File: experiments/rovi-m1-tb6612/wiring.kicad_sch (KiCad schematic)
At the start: 4 parts, among them M1 DC_MOTOR, U1 ESP32S3, U2 TB6612FNG

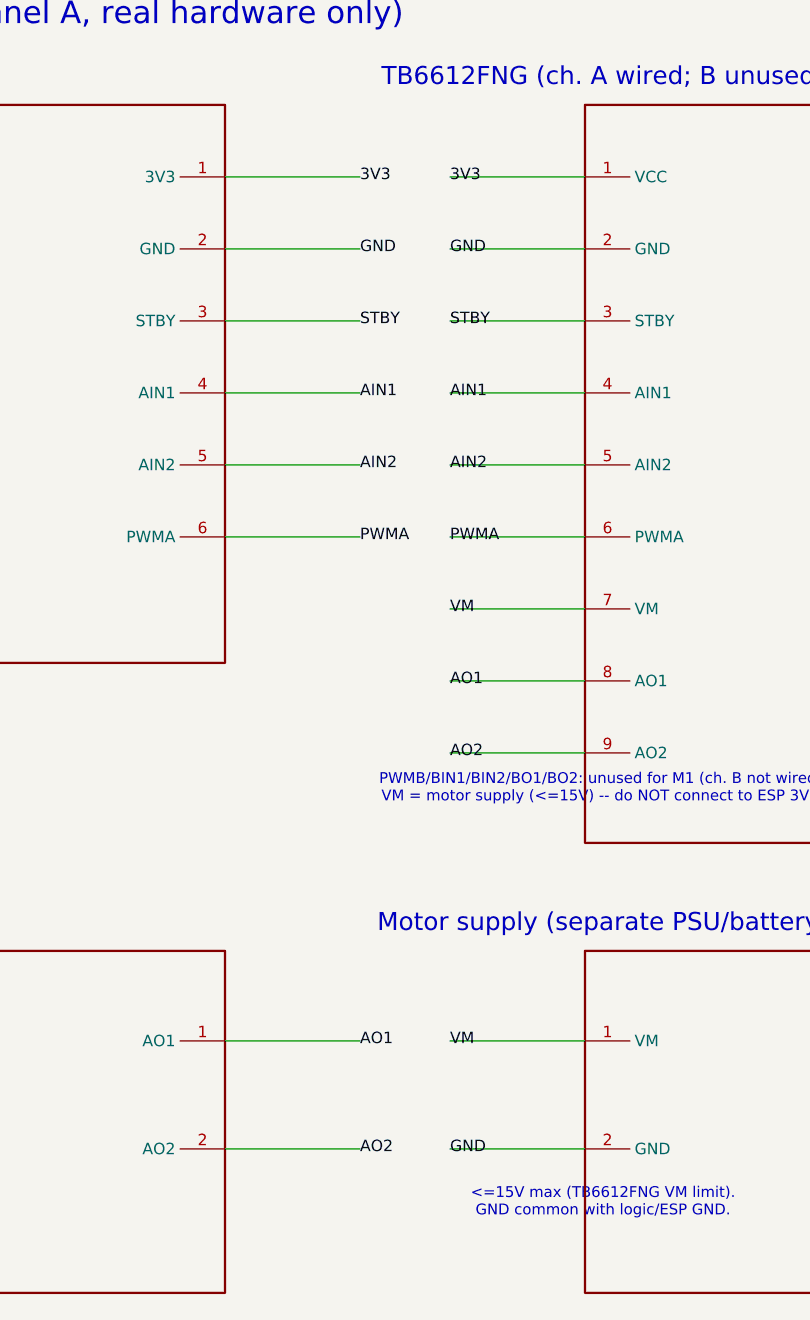
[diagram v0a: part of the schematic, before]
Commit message: wiring.kicad_sch: draw real wires between components, not just labels
The previous version connected pins purely via matching net labels
(electrically valid -- 0 ERC errors, confirmed real wire strokes in
the exported SVG) but never drew a line between the actual component
boxes. Opened in KiCad, that reads as floating labels near each pin,
not "wires connecting my components" -- a fair complaint.

Replaced the per-pin wire-to-label stubs with real point-to-point
wires: direct straight lines between ESP32S3 and TB6612FNG for the six
shared signals (3V3/GND/STBY/AIN1/AIN2/PWMA -- their pins happen to
share row Y-coordinates, so these are literal straight lines), and
bent multi-segment wires routing VM/AO1/AO2 from TB6612FNG down to the
Motor and Motor-supply boxes. GND is a 3-point net (ESP + TB6612FNG +
motor supply) so it gets an actual wire junction (visible dot) rather
than a fourth label.

Hit and diagnosed a real kicad-cli 9.0.6 ERC bug along the way: for a
direct multi-symbol wire with no label on it, `sch erc` always flags
the *first* point in a wire's `pts` list as "wire_dangling", regardless
of what's actually there -- confirmed by reversing the point order and
watching the false flag move with it. Isolated via a string of minimal
repro files (angle, pin type, rectangle coords, symbol name, instance
order, and UUIDs all ruled out one at a time) before finding the
workaround: a single label anywhere on a wire (even multi-segment,
junction-branched ones) satisfies the check for the whole connected
run. Kept one small label per net for this reason and because it aids
readability, even though the wires themselves now carry the
connection.

Verified: kicad-cli sch erc -- 0 errors, 0 dangling/unconnected
warnings (down from an intermediate 9 errors while chasing the false
positive). Re-rendered to PDF and visually confirmed continuous wire
lines run between every component, including the GND junction dot.

Co-Authored-By: Claude Sonnet 5 <noreply@anthropic.com>
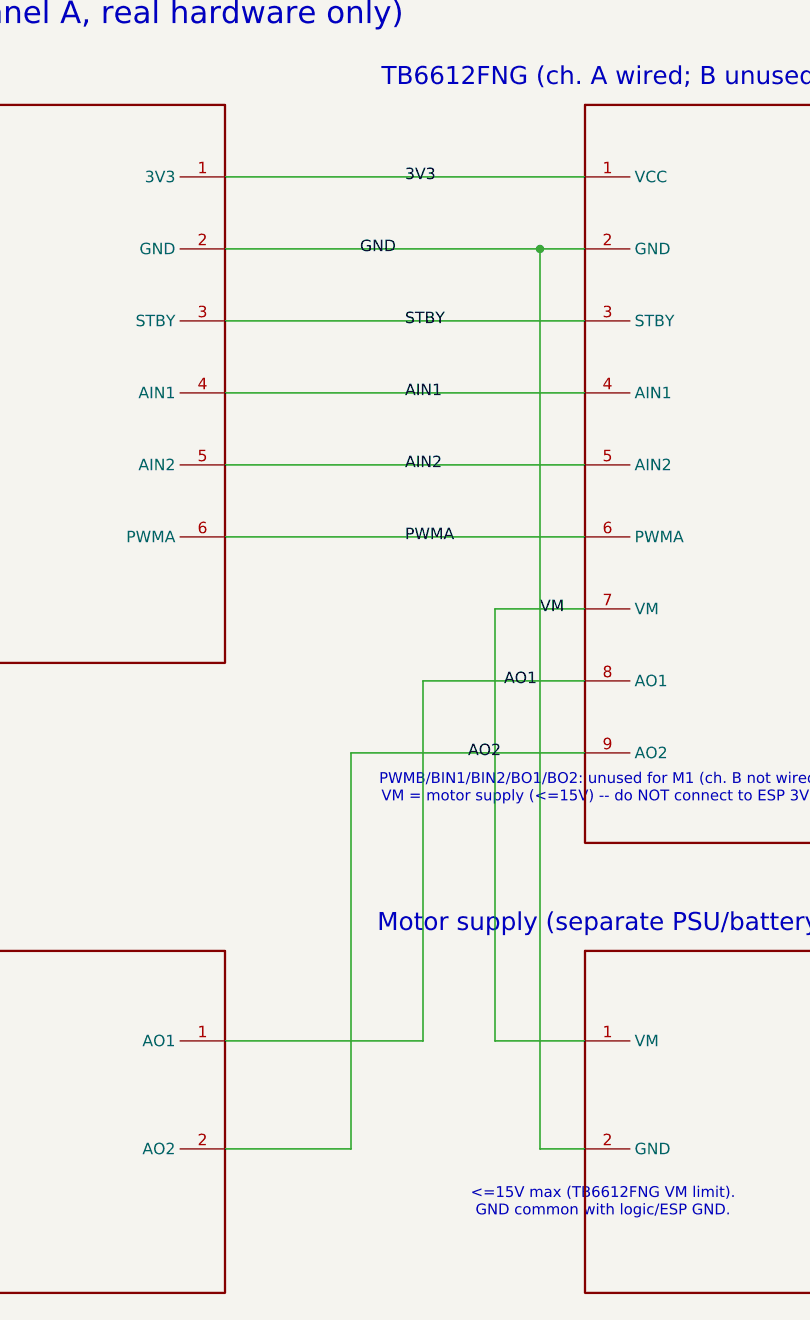
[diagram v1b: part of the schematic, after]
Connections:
- net VM is gone; now on net GND: PS1.1 (VM), U2.7 (VM)
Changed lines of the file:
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@@
 		(effects (font (size 2 2)))
-	)
-	(wire (pts (xy 70 26) (xy 85 26)) (stroke (width 0) (type default)))
-	(label "3V3" (at 85 26 0) (effects (font (size 1.27 1.27))))
-	(wire (pts (xy 70 34) (xy 85 34)) (stroke (width 0) (type default)))
-	(label "GND" (at 85 34 0) (effects (font (size 1.27 1.27))))
-	(wire (pts (xy 70 42) (xy 85 42)) (stroke (width 0) (type default)))
-	(label "STBY" (at 85 42 0) (effects (font (size 1.27 1.27))))
-	(wire (pts (xy 70 50) (xy 85 50)) (stroke (width 0) (type default)))
-	(label "AIN1" (at 85 50 0) (effects (font (size 1.27 1.27))))
-	(wire (pts (xy 70 58) (xy 85 58)) (stroke (width 0) (type default)))
-	(label "AIN2" (at 85 58 0) (effects (font (size 1.27 1.27))))
-	(wire (pts (xy 70 66) (xy 85 66)) (stroke (width 0) (type default)))
-	(label "PWMA" (at 85 66 0) (effects (font (size 1.27 1.27))))
-	(text "GPIO map:\nGPIO4=STBY  GPIO5=AIN1  GPIO6=AIN2\nGPIO7=PWMA (LEDC 20kHz)"
-		(at 22 70 0)
-		(effects (font (size 1.2 1.2)))
 	)
 	(symbol (lib_id "M1:TB6612FNG") (at 110 26 0) (unit 1) (in_bom yes) (on_board yes)
@@
 		(effects (font (size 2 2)))
 	)
-	(wire (pts (xy 110 26) (xy 95 26)) (stroke (width 0) (type default)))
-	(label "3V3" (at 95 26 0) (effects (font (size 1.27 1.27))))
-	(wire (pts (xy 110 34) (xy 95 34)) (stroke (width 0) (type default)))
-	(label "GND" (at 95 34 0) (effects (font (size 1.27 1.27))))
-	(wire (pts (xy 110 42) (xy 95 42)) (stroke (width 0) (type default)))
-	(label "STBY" (at 95 42 0) (effects (font (size 1.27 1.27))))
-	(wire (pts (xy 110 50) (xy 95 50)) (stroke (width 0) (type default)))
-	(label "AIN1" (at 95 50 0) (effects (font (size 1.27 1.27))))
-	(wire (pts (xy 110 58) (xy 95 58)) (stroke (width 0) (type default)))
-	(label "AIN2" (at 95 58 0) (effects (font (size 1.27 1.27))))
-	(wire (pts (xy 110 66) (xy 95 66)) (stroke (width 0) (type default)))
-	(label "PWMA" (at 95 66 0) (effects (font (size 1.27 1.27))))
-	(wire (pts (xy 110 74) (xy 95 74)) (stroke (width 0) (type default)))
-	(label "VM" (at 95 74 0) (effects (font (size 1.27 1.27))))
-	(wire (pts (xy 110 82) (xy 95 82)) (stroke (width 0) (type default)))
-	(label "AO1" (at 95 82 0) (effects (font (size 1.27 1.27))))
-	(wire (pts (xy 110 90) (xy 95 90)) (stroke (width 0) (type default)))
-	(label "AO2" (at 95 90 0) (effects (font (size 1.27 1.27))))
+	(text "GPIO map:\nGPIO4=STBY  GPIO5=AIN1  GPIO6=AIN2\nGPIO7=PWMA (LEDC 20kHz)"
+		(at 22 70 0)
+		(effects (font (size 1.2 1.2)))
+	)
 	(text "PWMB/BIN1/BIN2/BO1/BO2: unused for M1 (ch. B not wired).\nVM = motor supply (<=15V) -- do NOT connect to ESP 3V3!"
 		(at 112 94 0)
@@
 		(effects (font (size 2 2)))
 	)
-	(wire (pts (xy 70 122) (xy 85 122)) (stroke (width 0) (type default)))
-	(label "AO1" (at 85 122 0) (effects (font (size 1.27 1.27))))
-	(wire (pts (xy 70 134) (xy 85 134)) (stroke (width 0) (type default)))
-	(label "AO2" (at 85 134 0) (effects (font (size 1.27 1.27))))
 	(symbol (lib_id "M1:MOTORSUPPLY") (at 110 122 0) (unit 1) (in_bom yes) (on_board yes)
 		(property "Reference" "PS1" (at 130 132 0) (effects (font (size 1.27 1.27)) hide))
@@
 		(effects (font (size 2 2)))
 	)
-	(wire (pts (xy 110 122) (xy 95 122)) (stroke (width 0) (type default)))
-	(label "VM" (at 95 122 0) (effects (font (size 1.27 1.27))))
-	(wire (pts (xy 110 134) (xy 95 134)) (stroke (width 0) (type default)))
-	(label "GND" (at 95 134 0) (effects (font (size 1.27 1.27))))
 	(text "<=15V max (TB6612FNG VM limit).\nGND common with logic/ESP GND."
 		(at 112 140 0)
@@
 		(effects (font (size 1.5 1.5)))
 	)
+	(wire (pts (xy 70 26) (xy 110 26)) (stroke (width 0) (type default)))
+	(label "3V3" (at 90 26 0) (effects (font (size 1.27 1.27))))
+	(wire (pts (xy 70 34) (xy 105 34)) (stroke (width 0) (type default)))
+	(wire (pts (xy 105 34) (xy 110 34)) (stroke (width 0) (type default)))
+	(wire (pts (xy 105 34) (xy 105 134)) (stroke (width 0) (type default)))
+	(wire (pts (xy 105 134) (xy 110 134)) (stroke (width 0) (type default)))
+	(junction (at 105 34) (diameter 0) (color 0 0 0 0))
+	(label "GND" (at 85 34 0) (effects (font (size 1.27 1.27))))
+	(wire (pts (xy 70 42) (xy 110 42)) (stroke (width 0) (type default)))
+	(label "STBY" (at 90 42 0) (effects (font (size 1.27 1.27))))
+	(wire (pts (xy 70 50) (xy 110 50)) (stroke (width 0) (type default)))
+	(label "AIN1" (at 90 50 0) (effects (font (size 1.27 1.27))))
+	(wire (pts (xy 70 58) (xy 110 58)) (stroke (width 0) (type default)))
+	(label "AIN2" (at 90 58 0) (effects (font (size 1.27 1.27))))
+	(wire (pts (xy 70 66) (xy 110 66)) (stroke (width 0) (type default)))
+	(label "PWMA" (at 90 66 0) (effects (font (size 1.27 1.27))))
+	(wire (pts (xy 110 74) (xy 100 74)) (stroke (width 0) (type default)))
+	(wire (pts (xy 100 74) (xy 100 122)) (stroke (width 0) (type default)))
+	(wire (pts (xy 100 122) (xy 110 122)) (stroke (width 0) (type default)))
+	(label "VM" (at 105 74 0) (effects (font (size 1.27 1.27))))
+	(wire (pts (xy 110 82) (xy 92 82)) (stroke (width 0) (type default)))
+	(wire (pts (xy 92 82) (xy 92 122)) (stroke (width 0) (type default)))
+	(wire (pts (xy 92 122) (xy 70 122)) (stroke (width 0) (type default)))
+	(label "AO1" (at 101 82 0) (effects (font (size 1.27 1.27))))
+	(wire (pts (xy 110 90) (xy 84 90)) (stroke (width 0) (type default)))
+	(wire (pts (xy 84 90) (xy 84 134)) (stroke (width 0) (type default)))
+	(wire (pts (xy 84 134) (xy 70 134)) (stroke (width 0) (type default)))
+	(label "AO2" (at 97 90 0) (effects (font (size 1.27 1.27))))
 	(sheet_instances
 		(path "/" (page "1"))

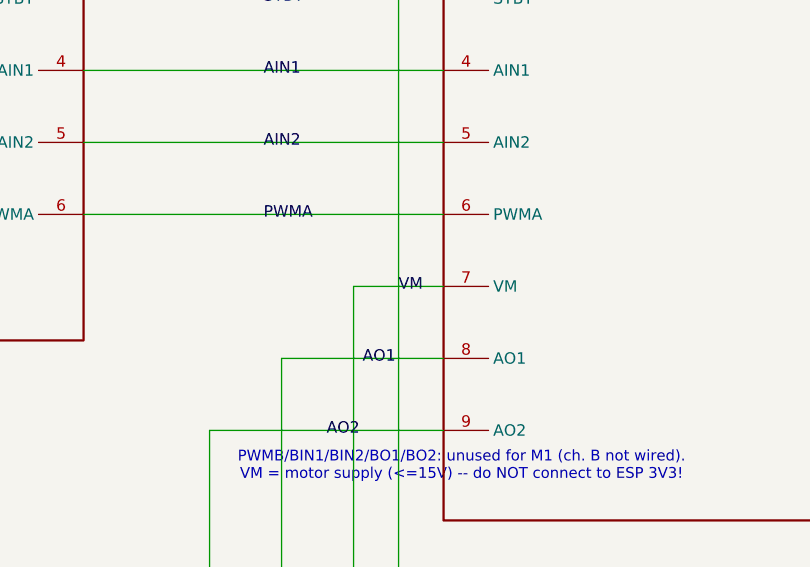
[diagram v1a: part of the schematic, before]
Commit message: Fix VM/GND short: VM label sat on top of the GND branch wire
Validated power-supply connectivity with the kicad-happy analyzer and
kicad-cli's own netlist export, per request. Found a real short: the
"VM" label was placed at (105,74), which is exactly on the GND
branch's vertical wire (x=105, spanning y=34 to y=134). The label
attached to that wire instead of the VM wire it was meant to annotate,
merging /VM and /GND into one 5-pin net -- electrically, the motor
supply's positive rail tied straight to ground.

Confirmed via kicad-cli sch export netlist (the authoritative
connectivity source, not a third-party reimplementation): before the
fix, net GND contained PS1.1(VM)+PS1.2+U1.2+U2.2+U2.7(VM) -- both VM
pins merged in. After moving the label to (103,74), off the GND
line: GND = {U1.2, U2.2, PS1.2} (3 pins, correct), VM = {U2.7, PS1.1}
(2 pins, correct) -- confirmed independently by both the raw netlist
export and the kicad-happy analyzer's net extraction, which agree
exactly.

Verified: kicad-cli sch erc still 0 errors, 0 connectivity warnings.
Re-rendered to PDF to confirm no visual regression.

Co-Authored-By: Claude Sonnet 5 <noreply@anthropic.com>
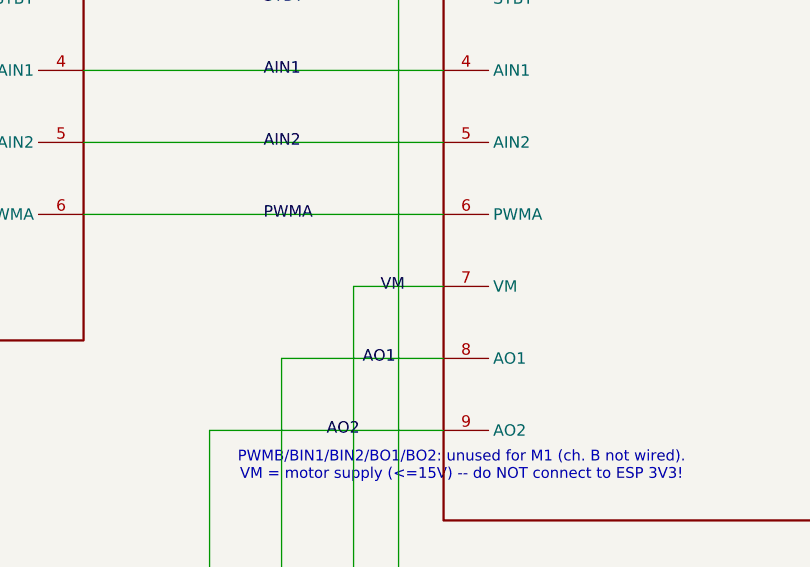
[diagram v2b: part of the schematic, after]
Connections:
- net GND: no longer PS1.1 (VM), U2.7 (VM)
- new net VM: PS1.1 (VM), U2.7 (VM)
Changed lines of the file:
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@@
 	(wire (pts (xy 100 74) (xy 100 122)) (stroke (width 0) (type default)))
 	(wire (pts (xy 100 122) (xy 110 122)) (stroke (width 0) (type default)))
-	(label "VM" (at 105 74 0) (effects (font (size 1.27 1.27))))
+	(label "VM" (at 103 74 0) (effects (font (size 1.27 1.27))))
 	(wire (pts (xy 110 82) (xy 92 82)) (stroke (width 0) (type default)))
 	(wire (pts (xy 92 82) (xy 92 122)) (stroke (width 0) (type default)))

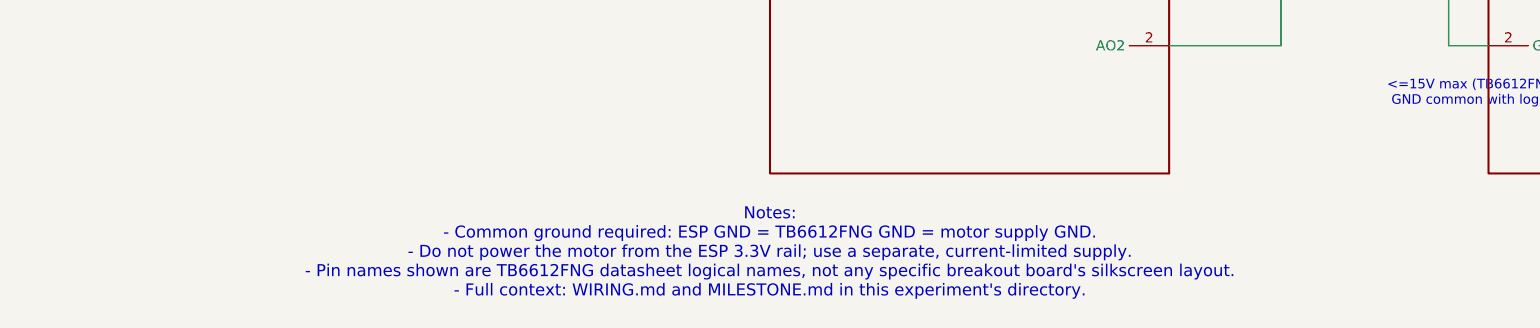
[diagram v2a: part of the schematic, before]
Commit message: Document: don't feed 5V into ESP 3V3, it's a regulated output
Answered the question directly (no, don't connect 5V USB to 3V3 --
it's the onboard LDO's regulated output, not an input; forcing 5V
onto it bypasses the regulator and would likely destroy the ESP32-S3
module, whose 3.3V rail has an absolute max around 3.6V). Confirmed
against the board photo: a 3-pin SOT-223 marked ...117 sits between
the USB-C connectors and the 3V3 pins in docs/reference/esp32-s3-n16r8/pinout.png.

Added the same caution to WIRING.md and the schematic's Notes text,
symmetric with the existing "don't power the motor from 3V3" warning
-- power the board via USB-C or the 5Vin pin instead.

Co-Authored-By: Claude Sonnet 5 <noreply@anthropic.com>
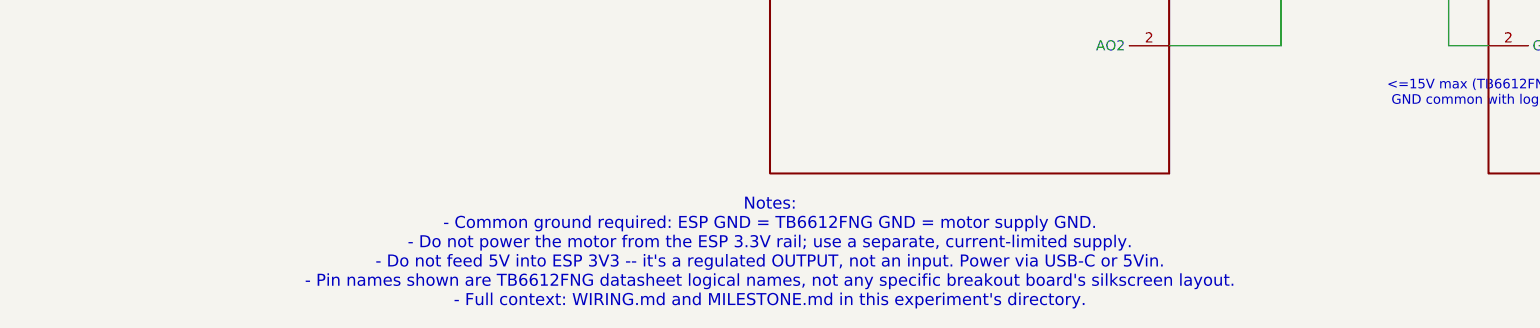
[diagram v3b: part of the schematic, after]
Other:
- note added: "Notes: - Common ground required: ESP GND = TB6612FNG GND = motor supply GND. - Do not power the motor from the ESP 3.3V rail; use a separate, current-limited supply. - Do not feed 5V into ESP 3V3 -- it's a regulated OUTPUT, not an input. Power via USB-C or 5Vin. - Pin names shown are TB6612FNG datasheet logical names, not any specific breakout board's silkscreen layout. - Full context: WIRING.md 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"
- note removed: "Notes: - Common ground required: ESP GND = TB6612FNG GND = motor supply GND. - Do not power the motor from the ESP 3.3V rail; use a separate, current-limited supply. - Pin names shown are TB6612FNG datasheet logical names, not any specific breakout board's silkscreen layout. - Full context: WIRING.md and MILESTONE.md in this experiment's directory."
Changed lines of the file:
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@@
 		(effects (font (size 1.2 1.2)))
 	)
-	(text "Notes:\n- Common ground required: ESP GND = TB6612FNG GND = motor supply GND.\n- Do not power the motor from the ESP 3.3V rail; use a separate, current-limited supply.\n- Pin names shown are TB6612FNG datasheet logical names, not any specific breakout board's silkscreen layout.\n- Full context: WIRING.md and MILESTONE.md in this experiment's directory."
+	(text "Notes:\n- Common ground required: ESP GND = TB6612FNG GND = motor supply GND.\n- Do not power the motor from the ESP 3.3V rail; use a separate, current-limited supply.\n- Do not feed 5V into ESP 3V3 -- it's a regulated OUTPUT, not an input. Power via USB-C or 5Vin.\n- Pin names shown are TB6612FNG datasheet logical names, not any specific breakout board's silkscreen layout.\n- Full context: WIRING.md and MILESTONE.md in this experiment's directory."
 		(at 20 160 0)
 		(effects (font (size 1.5 1.5)))
